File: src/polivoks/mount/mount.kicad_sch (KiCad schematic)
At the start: 22 parts, among them J1 FM_IN, J2 CV_IN, J3 INPUT, J4 BP_OUT, J5 LP_OUT, J6 01x14 Male, SW1 Switch

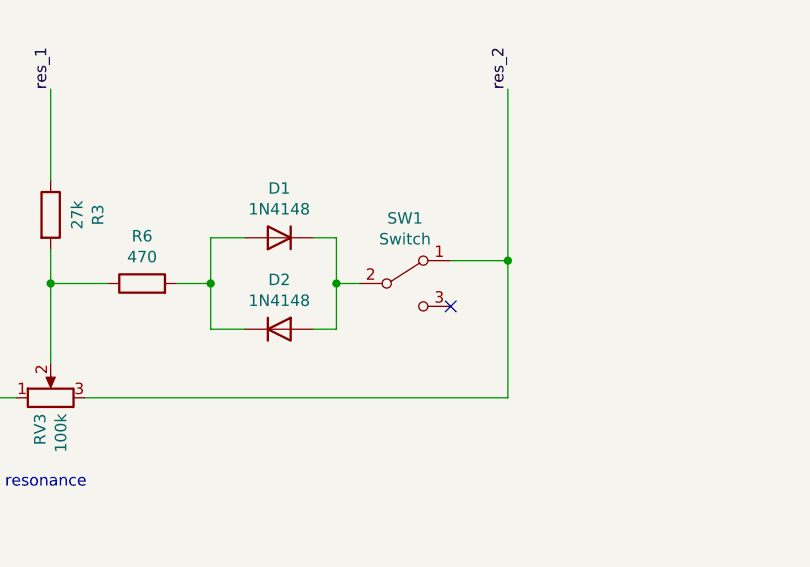
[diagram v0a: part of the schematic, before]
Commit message: update to Kicad8
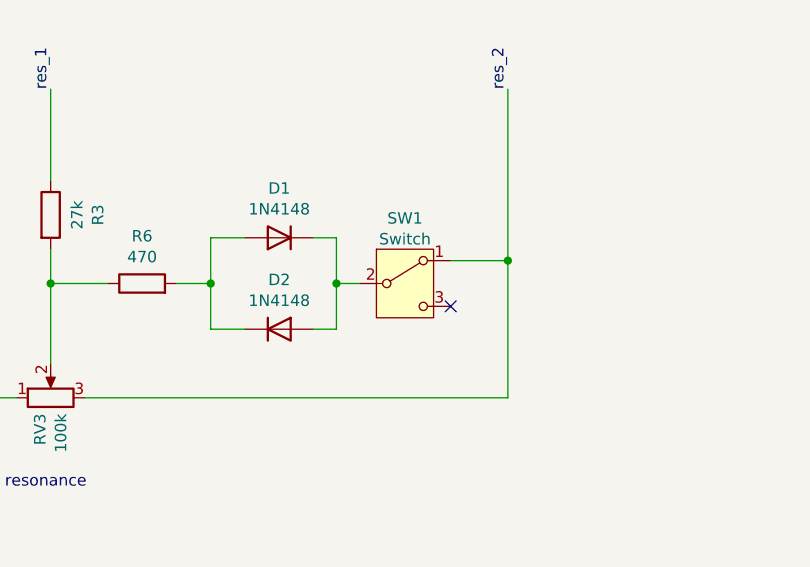
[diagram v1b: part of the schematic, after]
